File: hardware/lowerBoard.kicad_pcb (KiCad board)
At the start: 2 copper layers, 103 x 86.5 mm, 43 parts, among them J1 Screw_Terminal_01x02, J2 Screw_Terminal_01x04, J3 Screw_Terminal_01x06, J4 Screw_Terminal_01x06, J5 Screw_Terminal_01x04, J6 Screw_Terminal_01x06, J7 Screw_Terminal_01x06, J9 Conn_02x10_Odd_Even, K1 FINDER-34.51, K10 FINDER-34.51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

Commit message: continue to design lower pcb
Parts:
- removed J1: Screw_Terminal_01x02, TerminalBlock_MetzConnect:TerminalBlock_MetzConnect_Type059_RT06302HBWC_1x02_P3.50mm_Horizontal
- removed J2: Screw_Terminal_01x04, TerminalBlock_MetzConnect:TerminalBlock_MetzConnect_Type059_RT06304HBWC_1x04_P3.50mm_Horizontal
- removed J3: Screw_Terminal_01x06, TerminalBlock_MetzConnect:TerminalBlock_MetzConnect_Type059_RT06306HBWC_1x06_P3.50mm_Horizontal
- removed K1, K10, K11, K12, K13, K14, K15, K16, K2, K3, K4, K5, K6, K7, K8, K9: FINDER-34.51, Relay_THT:Relay_SPDT_Finder_34.51_Vertical
- removed U3: R-783.3-0.5, Converter_DCDC:Converter_DCDC_RECOM_R-78E-0.5_THT
- added U10: FINDER-43.41, Finder:FINDER-43.41, F.Cu at (174.2, 54.5)
- added U11: FINDER-43.41, Finder:FINDER-43.41, F.Cu at (184.8, 55.2)
- added U12: FINDER-43.41, Finder:FINDER-43.41, F.Cu at (195.0, 54.8)
- added U13: FINDER-43.41, Finder:FINDER-43.41, F.Cu at (205.2, 54.8)
- added U14: FINDER-43.41, Finder:FINDER-43.41, F.Cu at (206.2, 111.0)
- added U15: FINDER-43.41, Finder:FINDER-43.41, F.Cu at (195.8, 111.0)
- added U16: FINDER-43.41, Finder:FINDER-43.41, F.Cu at (185.2, 111.0)
- added U17: FINDER-43.41, Finder:FINDER-43.41, F.Cu at (174.8, 111.2)
- added U18: FINDER-43.41, Finder:FINDER-43.41, F.Cu at (144.8, 111.2)
- added U19: FINDER-43.41, Finder:FINDER-43.41, F.Cu at (134.5, 111.2)
- added U20: FINDER-43.41, Finder:FINDER-43.41, F.Cu at (124.0, 111.5)
- added U21: FINDER-43.41, Finder:FINDER-43.41, F.Cu at (113.5, 111.2)
- added U5: R-783.3-0.5, Converter_DCDC:Converter_DCDC_RECOM_R-78E-0.5_THT, F.Cu at (157.2, 96.2)
- added U6: FINDER-43.41, Finder:FINDER-43.41, F.Cu at (133.8, 55.0)
- added U7: FINDER-43.41, Finder:FINDER-43.41, F.Cu at (143.8, 55.2)
- added U8: FINDER-43.41, Finder:FINDER-43.41, F.Cu at (154.0, 55.0)
- added U9: FINDER-43.41, Finder:FINDER-43.41, F.Cu at (163.8, 55.0)
- J4: value Screw_Terminal_01x06 -> Screw_Terminal_01x09; footprint TerminalBlock_MetzConnect:TerminalBlock_MetzConnect_Type059_RT06306HBWC_1x06_P3.50mm_Horizontal -> TerminalBlock_RND:TerminalBlock_RND_205-00239_1x09_P5.08mm_Horizontal
- J5: value Screw_Terminal_01x04 -> Screw_Terminal_01x09; footprint TerminalBlock_MetzConnect:TerminalBlock_MetzConnect_Type059_RT06304HBWC_1x04_P3.50mm_Horizontal -> TerminalBlock_RND:TerminalBlock_RND_205-00239_1x09_P5.08mm_Horizontal
- J6, J7: value Screw_Terminal_01x06 -> Screw_Terminal_01x08; footprint TerminalBlock_MetzConnect:TerminalBlock_MetzConnect_Type059_RT06306HBWC_1x06_P3.50mm_Horizontal -> TerminalBlock_RND:TerminalBlock_RND_205-00238_1x08_P5.08mm_Horizontal
- moved C1 345.1 mm to (155.8, 106.0), turned to 180 degrees
- moved D3 341.4 mm to (161.8, 87.8)
- moved D4 340.2 mm to (164.8, 88.0)
- moved D5 339.4 mm to (167.5, 88.2)
- moved D7 338.3 mm to (199.5, 81.2), turned to 180 degrees
- moved D6 337.2 mm to (188.2, 81.2), turned to 180 degrees
- moved D2 333.6 mm to (147.5, 81.8), turned to 180 degrees
- moved D1 332.2 mm to (137.2, 81.5), turned to 180 degrees
- moved D12 330.5 mm to (168.5, 106.8)
- moved J6 330.4 mm to (202.0, 121.2)
- moved J5 327.7 mm to (166.4, 45.2)
- moved J7 323.7 mm to (153.5, 121.2)
- moved PS1 319.9 mm to (121.0, 52.2)
- moved J9 318.1 mm to (174.2, 81.8)
- moved D9 313.5 mm to (202.2, 84.5), turned to 0 degrees
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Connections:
- D1 pad 1: /12V -> /01
- D1 pad 2: /01 -> /GND
- D10 pad 1: /12V -> /10
- D10 pad 2: /10 -> /GND
- D11 pad 1: /12V -> /11
- D11 pad 2: /11 -> /GND
- D12 pad 1: /12V -> /12
- D12 pad 2: /12 -> /GND
- D13 pad 1: /12V -> /13
- D13 pad 2: /13 -> /GND
- D14 pad 1: /12V -> /15
- D14 pad 2: /15 -> /GND
- D15 pad 1: /12V -> /16
- D15 pad 2: /16 -> /GND
- D16 pad 1: /12V -> /14
- D16 pad 2: /14 -> /GND
- D2 pad 1: /12V -> /02
- D2 pad 2: /02 -> /GND
- D3 pad 1: /12V -> /03
- D3 pad 2: /03 -> /GND
- D4 pad 1: /12V -> /04
- D4 pad 2: /04 -> /GND
- D5 pad 1: /12V -> /05
- D5 pad 2: /05 -> /GND
- D6 pad 1: /12V -> /06
- D6 pad 2: /06 -> /GND
- D7 pad 1: /12V -> /07
- D7 pad 2: /07 -> /GND
- D8 pad 1: /12V -> /08
- D8 pad 2: /08 -> /GND
- D9 pad 1: /12V -> /09
- D9 pad 2: /09 -> /GND
- J4 pad 1: /relay05/sw -> Net-(J4-Pad1)
- J4 pad 2: NL -> Net-(J4-Pad2)
- J4 pad 3: /relay06/sw -> /relay01/sw
- J4 pad 4: NL -> /relay01/sw2
- J4 pad 5: /relay07/sw -> /relay02/sw
- J4 pad 6: NL -> /relay02/sw2
- J5 pad 1: /relay03/sw -> /relay04/sw2
- J5 pad 2: NL -> /relay05/sw
- J5 pad 3: /relay04/sw -> /relay05/sw2
- J5 pad 4: NL -> /relay06/sw
- J6 pad 1: /relay11/sw -> /relay09/sw
- J6 pad 2: NL -> /relay09/sw2
- J6 pad 3: /relay12/sw -> /relay10/sw
- J6 pad 4: NL -> /relay10/sw2
- J6 pad 5: /relay13/sw -> /relay11/sw
- J6 pad 6: NL -> /relay11/sw2
- J7 pad 1: /relay14/sw -> /relay13/sw
- J7 pad 2: NL -> /relay13/sw2
- J7 pad 3: /relay15/sw -> /relay14/sw
- J7 pad 4: NL -> /relay14/sw2
- J7 pad 5: /relay16/sw -> /relay15/sw
- J7 pad 6: NL -> /relay15/sw2
- J9 pad 1: /01 -> /08
- J9 pad 10: /10 -> /13
- J9 pad 11: /11 -> /03
- J9 pad 12: /12 -> /14
- J9 pad 13: /13 -> /02
- J9 pad 14: /14 -> /15
- J9 pad 15: /15 -> /01
- J9 pad 2: /02 -> /09
- J9 pad 3: /03 -> /07
- J9 pad 4: /04 -> /10
- J9 pad 5: /05 -> /06
- J9 pad 6: /06 -> /11
- J9 pad 7: /07 -> /05
- J9 pad 8: /08 -> /12
- J9 pad 9: /09 -> /04
- PS1 pad 1: 230V -> Net-(J4-Pad2)
- PS1 pad 2: NL -> Net-(J4-Pad1)
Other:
- outline, holes or cut-outs redrawn

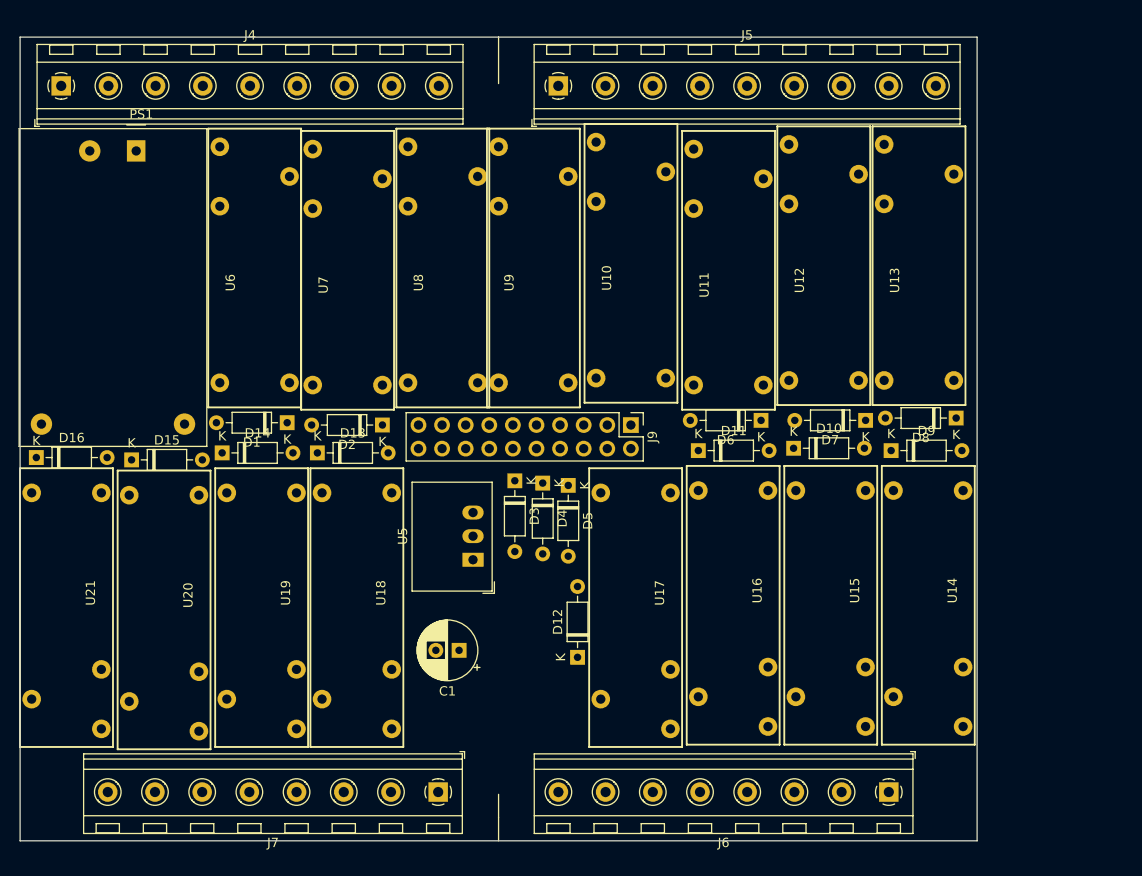
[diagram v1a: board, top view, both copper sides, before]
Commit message: move on to 16A relays
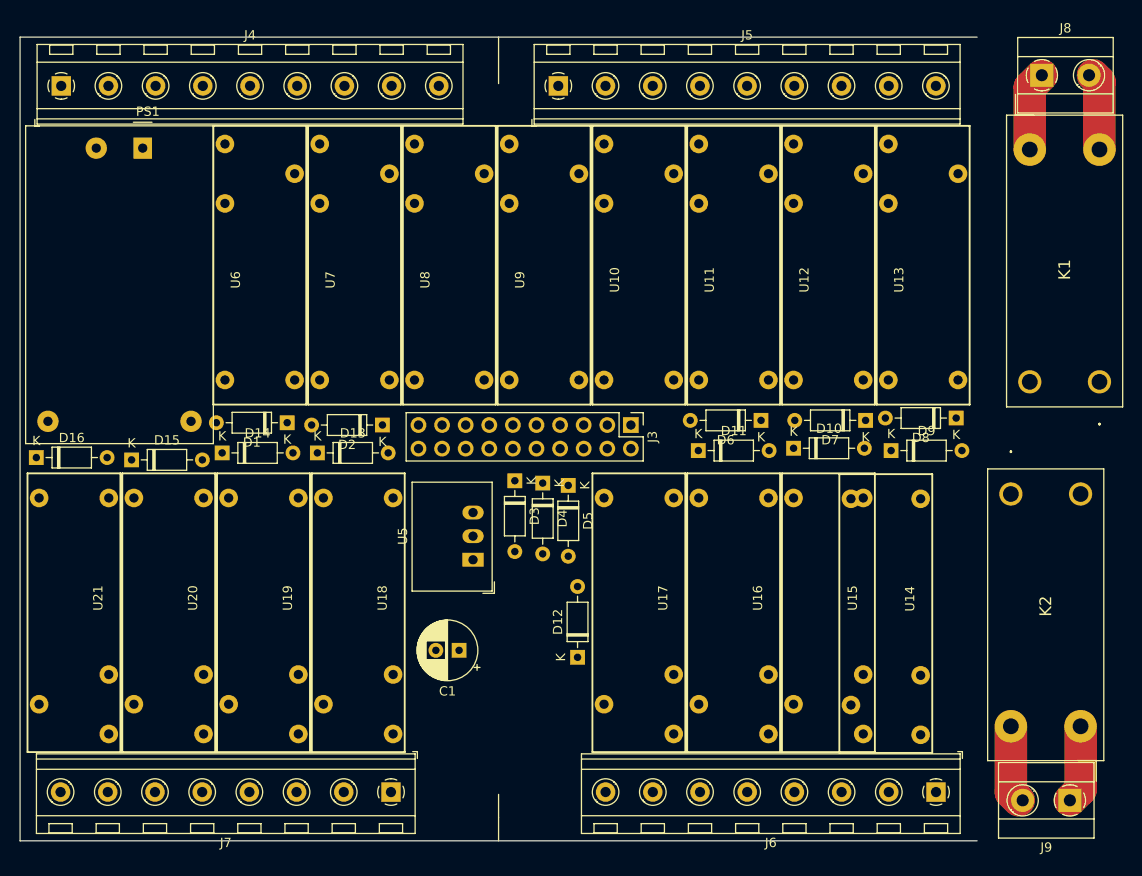
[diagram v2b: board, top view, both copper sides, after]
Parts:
- added J8: Screw_Terminal_01x02, TerminalBlock_MetzConnect:TerminalBlock_MetzConnect_Type101_RT01602HBWC_1x02_P5.08mm_Horizontal, F.Cu at (218.5, 44.1)
- added J9: Screw_Terminal_01x02, TerminalBlock_MetzConnect:TerminalBlock_MetzConnect_Type101_RT01602HBWC_1x02_P5.08mm_Horizontal, F.Cu at (221.5, 122.1)
- added K1: 45.31.7.024.0310, Finder:finder-45.31.7.024.0310, F.Cu at (224.7, 77.1)
- added K2: 45.31.7.024.0310, Finder:finder-45.31.7.024.0310, F.Cu at (215.1, 89.2)
- C1: value 100µF -> 220µF
- U10, U11, U12, U13, U14, U15, U16, U17, U18, U19, U20, U21, U6, U7, U8, U9: footprint Finder:FINDER-43.41 -> Finder:finder-43.41
- moved J6 5.08 mm to (207.1, 121.2)
- moved J7 5.08 mm to (148.4, 121.2)
- moved U14 4.66 mm to (201.7, 111.9)
- moved U9 1.19 mm to (164.9, 54.7)
- moved U21 0.97 mm to (114.3, 111.8)
- moved U7 0.93 mm to (144.5, 54.7)
- moved U10 0.87 mm to (175.1, 54.7)
- moved U15 0.84 mm to (195.5, 111.8)
- moved U16 0.80 mm to (185.3, 111.8)
- moved U11 0.78 mm to (185.3, 54.7)
- moved PS1 0.76 mm to (121.7, 52.0)
- moved U8 0.76 mm to (154.7, 54.7)
- moved U17 0.65 mm to (175.1, 111.8)
- moved U6 0.63 mm to (134.3, 54.7)
- moved U19 0.59 mm to (134.7, 111.8)
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- renumbered J9 to J3
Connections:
- U10 pad 12: Net-(U10-Pad12) -> (no net)
- U11 pad 12: Net-(U11-Pad12) -> (no net)
- U12 pad 12: Net-(U12-Pad12) -> (no net)
- U13 pad 12: Net-(U13-Pad12) -> (no net)
- U14 pad 12: Net-(U14-Pad12) -> (no net)
- U15 pad 12: Net-(U15-Pad12) -> (no net)
- U16 pad 12: Net-(U16-Pad12) -> (no net)
- U17 pad 12: Net-(U17-Pad12) -> (no net)
- U18 pad 12: Net-(U18-Pad12) -> (no net)
- U19 pad 12: Net-(U19-Pad12) -> (no net)
- U20 pad 12: Net-(U20-Pad12) -> (no net)
- U21 pad 12: Net-(U21-Pad12) -> (no net)
- U6 pad 12: Net-(U6-Pad12) -> (no net)
- U7 pad 12: Net-(U7-Pad12) -> (no net)
- U8 pad 12: Net-(U8-Pad12) -> (no net)
- U9 pad 12: Net-(U9-Pad12) -> (no net)
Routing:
- net Net-(J8-Pad1): track 0.00 -> 8.54 mm
- net Net-(J9-Pad1): track 0.00 -> 8.45 mm
- net Net-(J9-Pad2): track 0.00 -> 8.33 mm
- net Net-(J8-Pad2): track 0.00 -> 8.29 mm
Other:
- net class 230V added: clearance 2, trace_width 3.5, via_dia 2.5, via_drill 1
